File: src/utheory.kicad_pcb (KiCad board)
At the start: 2 copper layers, 28 parts, among them J1 USB_B_Micro, Q1 FDN340P, Q2 MMBT3904, Q3 MMBT3904, U1 ESP32-PICO-D4, U2 ADG417BN, U3 SL4054ST25P, U4 TLV70012_SOT23-5, U5 JTAG, U6 FT231XS

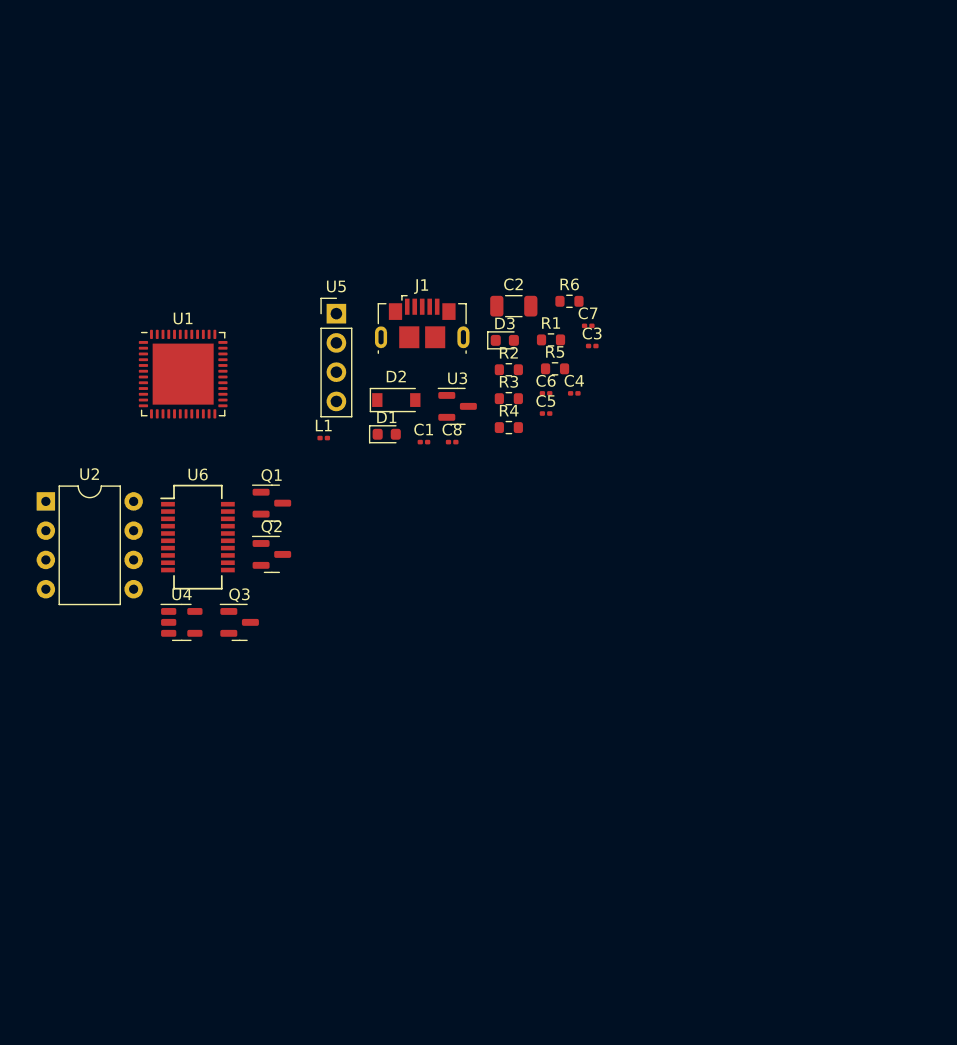
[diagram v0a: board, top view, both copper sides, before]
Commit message: schematic more filled out
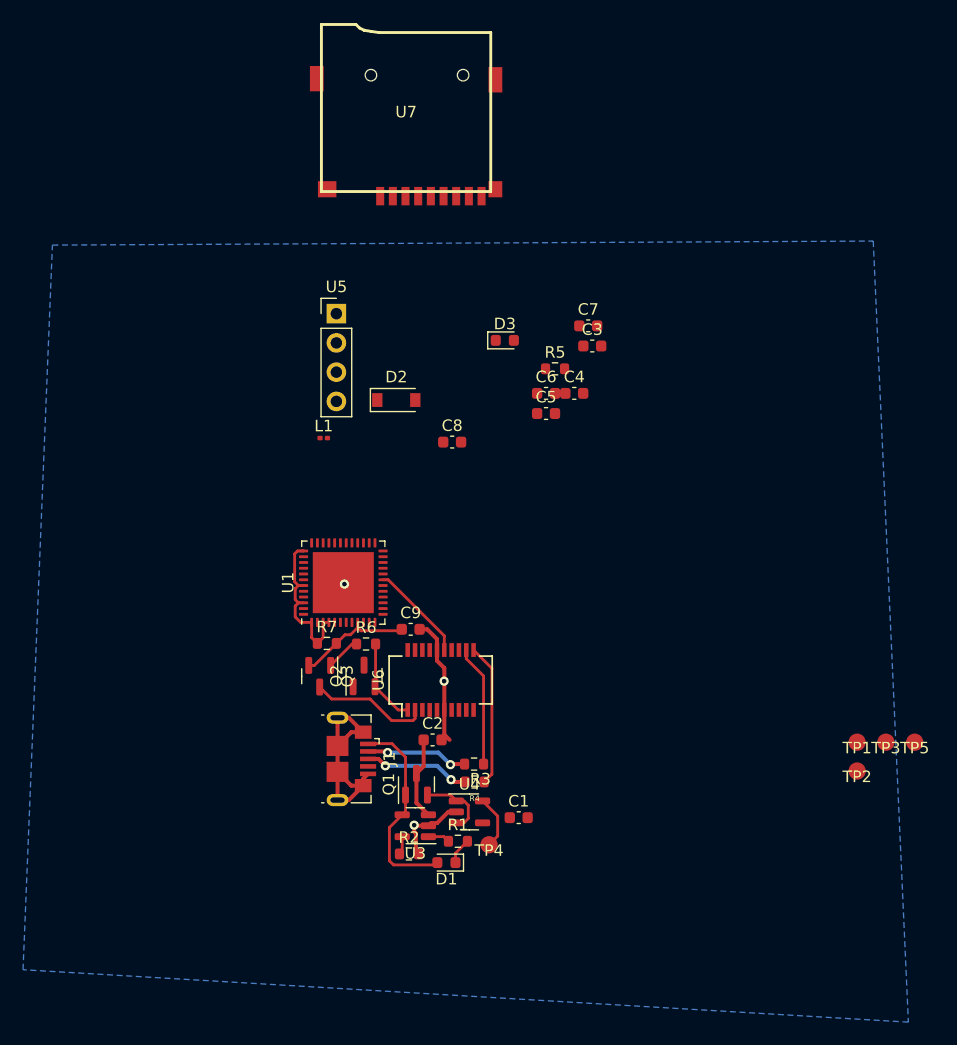
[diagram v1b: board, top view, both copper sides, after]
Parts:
- removed U2: ADG417BN, Package_DIP:DIP-8_W7.62mm
- added C9: 2.7pF, Capacitor_SMD:C_0603_1608Metric, F.Cu at (177.3, 109.5)
- added R7: 10k, Resistor_SMD:R_0603_1608Metric, F.Cu at (170.1, 110.8)
- added TP1: gndct, microsd:testpad, F.Cu at (216.1, 119.3)
- added TP2: rxdct, microsd:testpad, F.Cu at (216.1, 121.8)
- added TP3: txdct, microsd:testpad, F.Cu at (218.6, 119.3)
- added TP4: TestPoint, microsd:testpad, F.Cu at (184.2, 128.2)
- added TP5: TestPoint, microsd:testpad, F.Cu at (221.1, 119.3)
- added U7: MicroSD_SPI_CD, microsd:GCT-MEM2055-00-190-01-A, F.Cu at (176.9, 72.8)
- C1, C3, C4, C5, C6, C7, C8: footprint Capacitor_SMD:C_0201_0603Metric -> Capacitor_SMD:C_0603_1608Metric
- C2: footprint Capacitor_SMD:C_1206_3216Metric -> Capacitor_SMD:C_0603_1608Metric
- U3: footprint Package_TO_SOT_SMD:SOT-23 -> Package_TO_SOT_SMD:SOT-23-5
- moved R1 44.3 mm to (181.4, 128.0)
- moved R2 42.9 mm to (177.2, 129.1)
- moved C2 38.3 mm to (179.2, 119.2)
- moved J1 38.3 mm to (172.2, 120.8), turned to 270 degrees
- moved D1 37.5 mm to (180.4, 129.8), turned to 180 degrees
- moved U3 36.6 mm to (177.8, 126.6), turned to 180 degrees
- moved R6 34.6 mm to (173.5, 110.8)
- moved C1 33.6 mm to (186.7, 125.9)
- moved R3 31.9 mm to (182.8, 121.2), turned to 180 degrees
- moved R4 30.9 mm to (182.9, 122.8), turned to 180 degrees
- moved U4 29.9 mm to (182.4, 125.4)
- moved Q1 27.4 mm to (177.8, 123.0), turned to 90 degrees
- moved U6 24.4 mm to (179.9, 114.0), turned to 90 degrees
- moved U1 22.8 mm to (171.5, 105.5), turned to 90 degrees
- moved Q2 13.2 mm to (173.3, 113.6), turned to 90 degrees
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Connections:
- U1 pad 34: BLUE -> CS
- U1 pad 35: GREEN -> CLK
- U1 pad 36: RED -> MOSI
- U1 pad 38: Net-(U1-Pad38) -> MISO
- U1 pad 49: Net-(U1-Pad49) -> GND
- U1 pad 9: Net-(U1-Pad9) -> EN
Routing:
- net GND: track 0.00 -> 37.6 mm, vias 0 -> 3
- net +3V3: track 0.00 -> 27.1 mm
- net Net-(D1-Pad2): track 0.00 -> 19.7 mm
- net Net-(R4-Pad1): track 0.00 -> 12.4 mm
- net Net-(R3-Pad1): track 0.00 -> 10.5 mm
- net Net-(Q3-Pad3): track 0.00 -> 10.3 mm
- net EN: track 0.00 -> 10.1 mm
- net D+: track 0.00 -> 9.25 mm, vias 0 -> 2
- net D-: track 0.00 -> 8.94 mm, vias 0 -> 2
- net Net-(Q2-Pad2): track 0.00 -> 7.41 mm
- net VBAT: track 0.00 -> 7.29 mm
- net Net-(C1-Pad1): track 0.00 -> 6.97 mm
- net Net-(Q3-Pad1): track 0.00 -> 3.02 mm
- net Net-(D1-Pad1): track 0.00 -> 2.28 mm
- net Net-(R1-Pad1): track 0.00 -> 1.90 mm
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- added copper zone on B.Cu, net GND
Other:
- net class thicc added: clearance 0.25, trace_width 0.35, via_dia 0.8, via_drill 0.4

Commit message: pcb v1
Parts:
- removed TP1: gndct, microsd:testpad
- removed U5: JTAG, Connector_PinHeader_2.54mm:PinHeader_1x04_P2.54mm_Vertical
- L1: footprint Inductor_SMD:L_0201_0603Metric -> Inductor_SMD:L_0603_1608Metric
- moved U7 50.5 mm to (195.7, 119.6), turned to 270 degrees
- moved TP3 45.5 mm to (173.2, 116.5)
- moved TP5 43.6 mm to (177.6, 116.2)
- moved TP2 41.3 mm to (175.2, 115.9)
- moved C4 40.6 mm to (181.8, 128.4), turned to 180 degrees
- moved C6 38.5 mm to (181.8, 126.9)
- moved C3 38.0 mm to (175.2, 118.5), turned to 90 degrees
- moved L1 37.2 mm to (185.0, 126.9), turned to 180 degrees
- moved C7 35.3 mm to (181.2, 116.5), turned to 180 degrees
- moved C5 34.8 mm to (183.5, 125.2), turned to 180 degrees
- moved D2 33.4 mm to (167.0, 121.8), turned to 90 degrees
- moved C8 31.8 mm to (180.2, 125.1)
- moved R5 28.7 mm to (184.0, 115.0), turned to 180 degrees
- moved R7 25.6 mm to (189.9, 127.0)
- moved U1 24.6 mm to (189.7, 122.0)
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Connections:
- R3 pad 1: Net-(R3-Pad1) -> D-
- R4 pad 1: Net-(R4-Pad1) -> D+
- U6 pad 11: Net-(R4-Pad1) -> D+
- U6 pad 12: Net-(R3-Pad1) -> D-
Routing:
- net +3V3: track 27.1 -> 76.6 mm, vias 0 -> 6
- net GND: track 37.6 -> 56.7 mm, vias 3 -> 5
- net TXD: track 0.00 -> 17.3 mm, vias 0 -> 2
- net RXD: track 0.00 -> 15.1 mm, vias 0 -> 2
- net MISO: track 0.00 -> 14.5 mm, vias 0 -> 2
- net MOSI: track 0.00 -> 14.0 mm, vias 0 -> 2
- net CLK: track 0.00 -> 12.7 mm, vias 0 -> 2
- net EN: track 10.1 -> 22.7 mm, vias 0 -> 1
- net Net-(R4-Pad1): track 12.4 -> 0.00 mm
- net Net-(R3-Pad1): track 10.5 -> 0.00 mm
- net Net-(C7-Pad1): track 0.00 -> 9.95 mm, vias 0 -> 2
- net CS: track 0.00 -> 9.55 mm, vias 0 -> 2
- net IO0: track 0.00 -> 9.53 mm, vias 0 -> 2
- net Net-(C1-Pad1): track 6.97 -> 15.0 mm, vias 0 -> 2
- net D-: track 8.94 -> 13.9 mm
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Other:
- net class Default: via_dia 0.8 -> 0.6
- net class thicc: trace_width 0.35 -> 0.3; via_dia 0.8 -> 0.6
- board text added: "."
- board text added: "3v3"
- board text added: "GND"
- board text added: "RX"
- board text added: "TX"

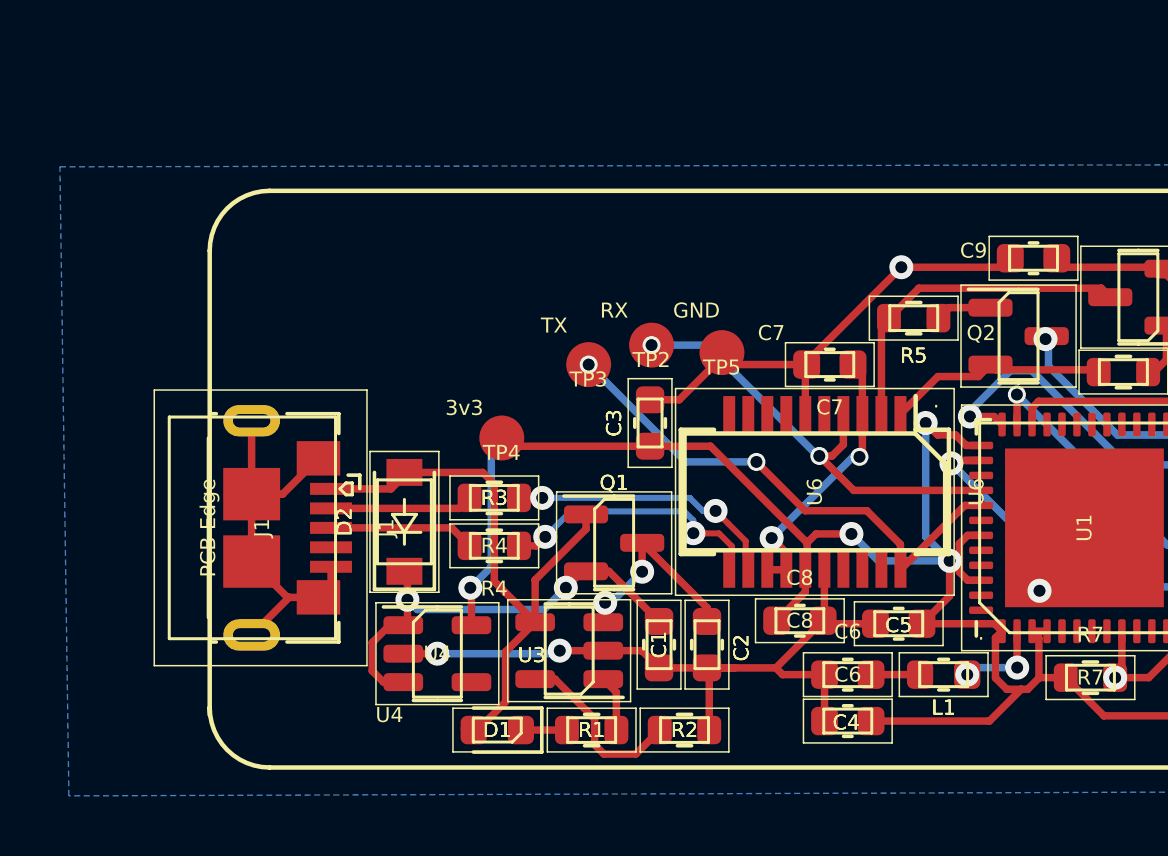
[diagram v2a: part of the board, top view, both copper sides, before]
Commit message: added antenna
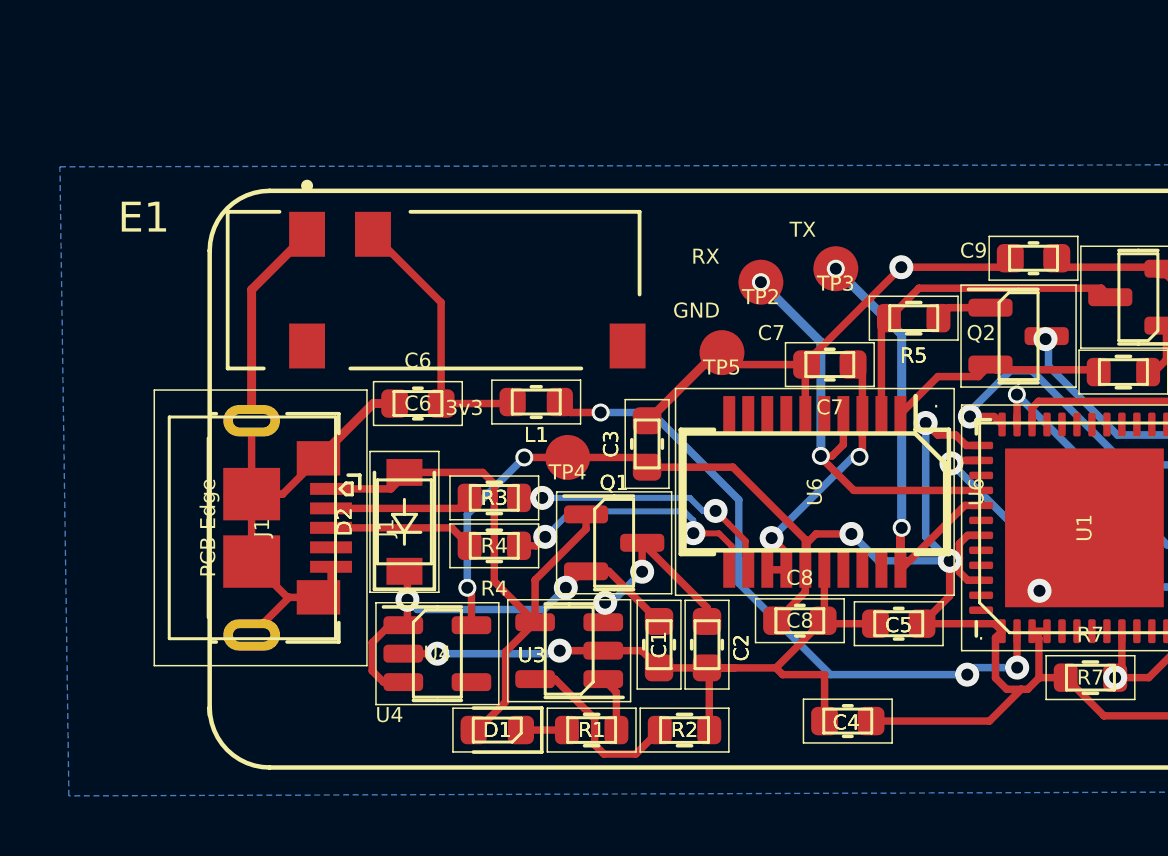
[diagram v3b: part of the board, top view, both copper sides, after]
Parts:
- added E1: PRO-OB-440, PRO-0B-440:ANT_PRO-OB-440, F.Cu at (163.8, 112.2)
- moved C6 17.0 mm to (167.4, 117.8)
- moved L1 16.4 mm to (171.4, 117.8)
- moved TP3 8.85 mm to (181.4, 113.3)
- moved TP2 4.21 mm to (178.9, 113.8)
- moved TP4 2.29 mm to (172.4, 119.7)
- moved C3 0.71 mm to (175.1, 119.2)
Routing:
- net Net-(L1-Pad1): track 2.98 -> 22.0 mm, vias 2 -> 3
- net GND: track 56.7 -> 67.3 mm
- net Net-(C6-Pad2): track 1.64 -> 9.00 mm
- net TXD: track 17.3 -> 14.6 mm
- net RXD: track 15.1 -> 14.5 mm
- net +3V3: track 76.6 -> 76.1 mm, vias 6 -> 7
